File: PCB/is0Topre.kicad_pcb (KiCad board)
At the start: 2 copper layers, 28.6 x 49.7 mm, 32 parts, among them SW1 SW_Push, SW2 EC_SW, U1 ATmega32U4-M, U2 OPA350, Y1 16MHz

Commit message: Updated pic and production to add logo
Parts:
- added G***: LOGO, cipulot_parts:IronMan_small, B.Cu at (110.5, 46.5)

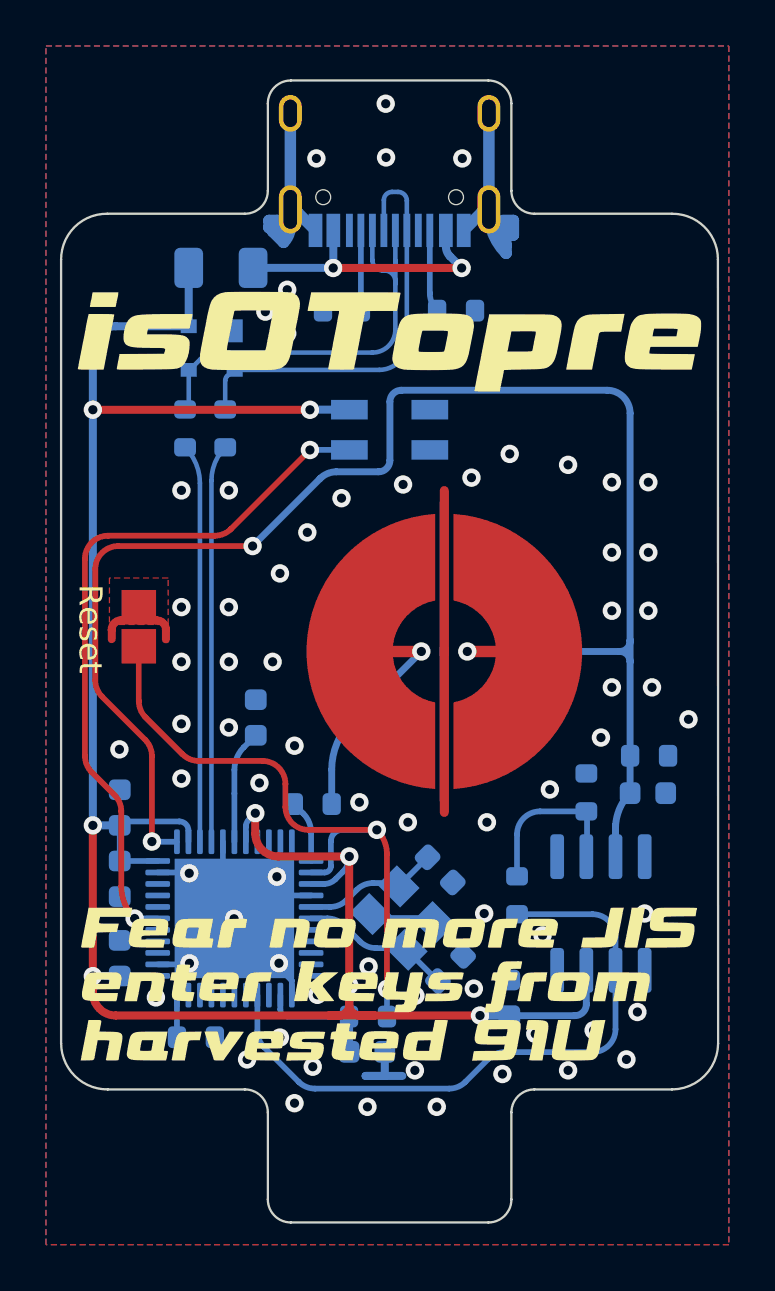
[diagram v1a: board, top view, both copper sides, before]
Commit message: Update to add tape silkscreen
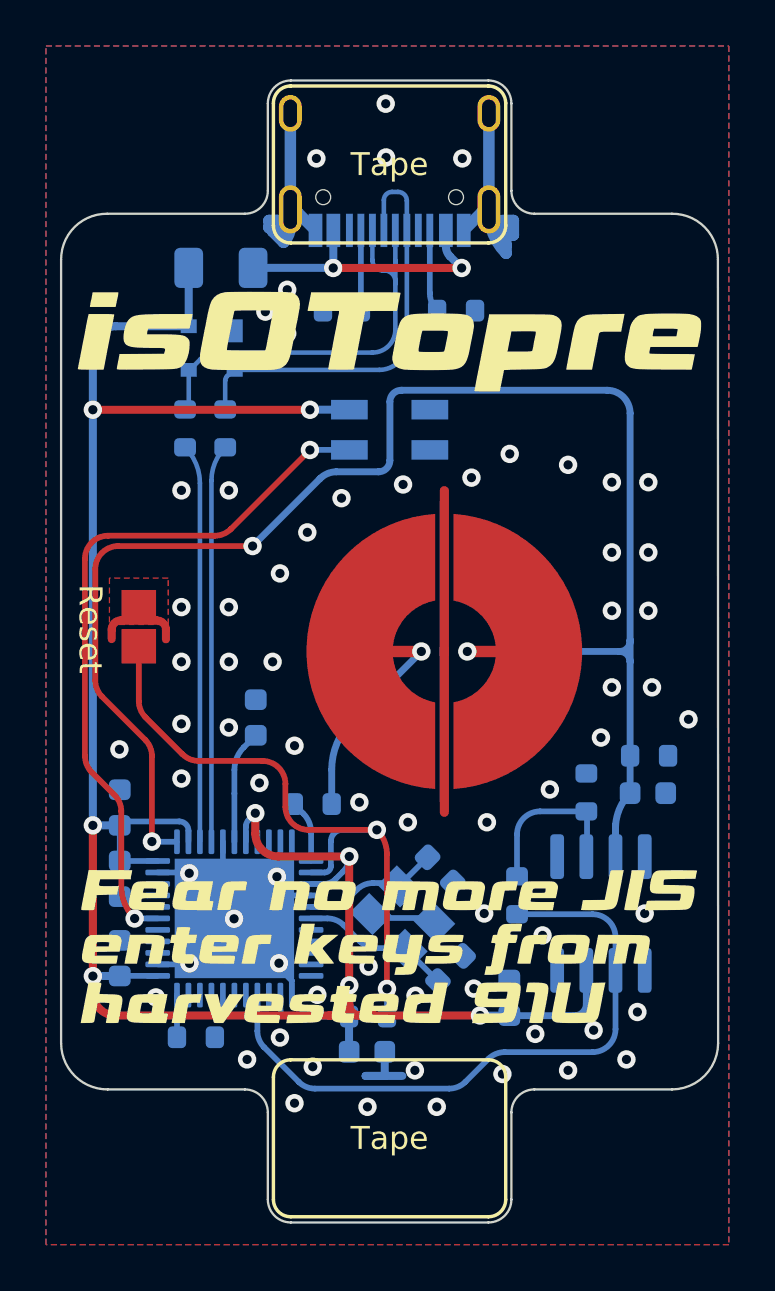
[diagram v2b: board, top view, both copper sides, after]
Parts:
- moved G*** 1.63 mm to (99.5, 71.9)
- moved G*** 1.63 mm to (99.5, 74.4)
- moved G*** 1.63 mm to (99.5, 77.0)
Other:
- board text added: "Tape"
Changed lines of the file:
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@@
   )
   (footprint "LOGO" (layer "F.Cu")
-    (at 99.545928 73.509504)
+    (at 99.545928 71.878991)
     (attr board_only exclude_from_pos_files exclude_from_bom)
     (fp_text reference "G***" (at 0 0) (layer "F.SilkS") hide
@@
   )
   (footprint "LOGO" (layer "F.Cu")
-    (at 99.545928 76.070754)
+    (at 99.545928 74.440241)
     (attr board_only exclude_from_pos_files exclude_from_bom)
     (fp_text reference "G***" (at 0 0) (layer "F.SilkS") hide
@@
   )
   (footprint "LOGO" (layer "F.Cu")
-    (at 99.545928 78.630754)
+    (at 99.545928 77.000241)
     (attr board_only exclude_from_pos_files exclude_from_bom)
     (fp_text reference "G***" (at 0 0) (layer "F.SilkS") hide
@@
     )
   )
+  (gr_arc (start 94.48875 37.64125) (mid 94.708883 37.10903) (end 95.241578 36.890071) (layer "F.SilkS") (width 0.15))
+  (gr_line (start 103.841578 36.890071) (end 95.241578 36.890071) (layer "F.SilkS") (width 0.15))
+  (gr_line (start 104.59875 42.966962) (end 104.59875 37.64125) (layer "F.SilkS") (width 0.15))
+  (gr_arc (start 95.245922 86.10125) (mid 94.711324 85.882899) (end 94.48875 85.350071) (layer "F.SilkS") (width 0.15))
+  (gr_arc (start 94.48875 80.024359) (mid 94.707661 79.492691) (end 95.2384 79.271538) (layer "F.SilkS") (width 0.15))
+  (gr_line (start 95.2384 79.271538) (end 103.845929 79.271538) (layer "F.SilkS") (width 0.15))
+  (gr_arc (start 104.59875 42.966962) (mid 104.379839 43.49863) (end 103.8491 43.719783) (layer "F.SilkS") (width 0.15))
+  (gr_line (start 104.59875 80.021188) (end 104.59875 85.350071) (layer "F.SilkS") (width 0.15))
+  (gr_line (start 94.48875 42.970133) (end 94.48875 37.64125) (layer "F.SilkS") (width 0.15))
+  (gr_arc (start 95.241571 43.719783) (mid 94.709893 43.500876) (end 94.48875 42.970133) (layer "F.SilkS") (width 0.15))
+  (gr_arc (start 103.841578 36.890071) (mid 104.376144 37.108436) (end 104.59875 37.64125) (layer "F.SilkS") (width 0.15))
+  (gr_line (start 95.245922 86.10125) (end 103.845922 86.10125) (layer "F.SilkS") (width 0.15))
+  (gr_arc (start 104.59875 85.350071) (mid 104.37862 85.882288) (end 103.845922 86.10125) (layer "F.SilkS") (width 0.15))
+  (gr_line (start 94.48875 80.024359) (end 94.48875 85.350071) (layer "F.SilkS") (width 0.15))
+  (gr_line (start 103.8491 43.719783) (end 95.241571 43.719783) (layer "F.SilkS") (width 0.15))
+  (gr_arc (start 103.845929 79.271538) (mid 104.377605 79.490442) (end 104.59875 80.021188) (layer "F.SilkS") (width 0.15))
   (gr_line (start 93.245927 42.449999) (end 87.258428 42.449999) (layer "Edge.Cuts") (width 0.1))
   (gr_line (start 95.245922 86.350071) (end 103.845922 86.350071) (layer "Edge.Cuts") (width 0.1))
@@
     (effects (font (size 1 1) (thickness 0.15)) (justify mirror))
   )
+  (gr_text "Tape\n" (at 99.541578 40.304106) (layer "F.SilkS")
+    (effects (font (size 1 1) (thickness 0.15)))
+  )
   (gr_text "Reset" (at 86.517178 60.521801 270) (layer "F.SilkS")
     (effects (font (size 1 1) (thickness 0.15)))
   )
+  (gr_text "Tape" (at 99.541578 82.68563) (layer "F.SilkS")
+    (effects (font (size 1 1) (thickness 0.15)))
+  )

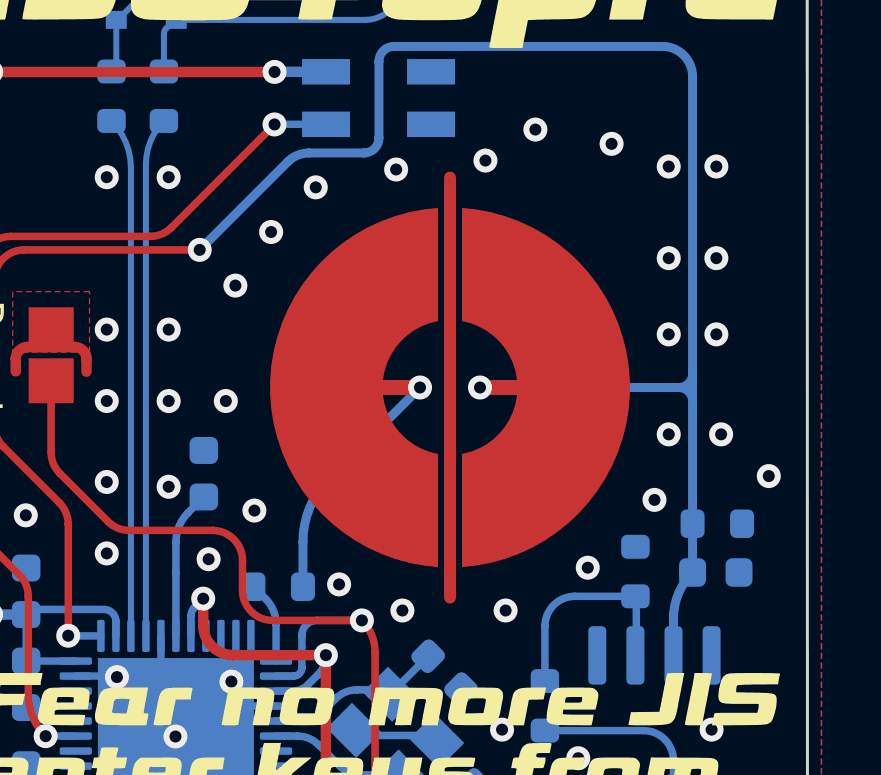
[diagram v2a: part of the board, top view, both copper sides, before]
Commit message: Update for 3d models
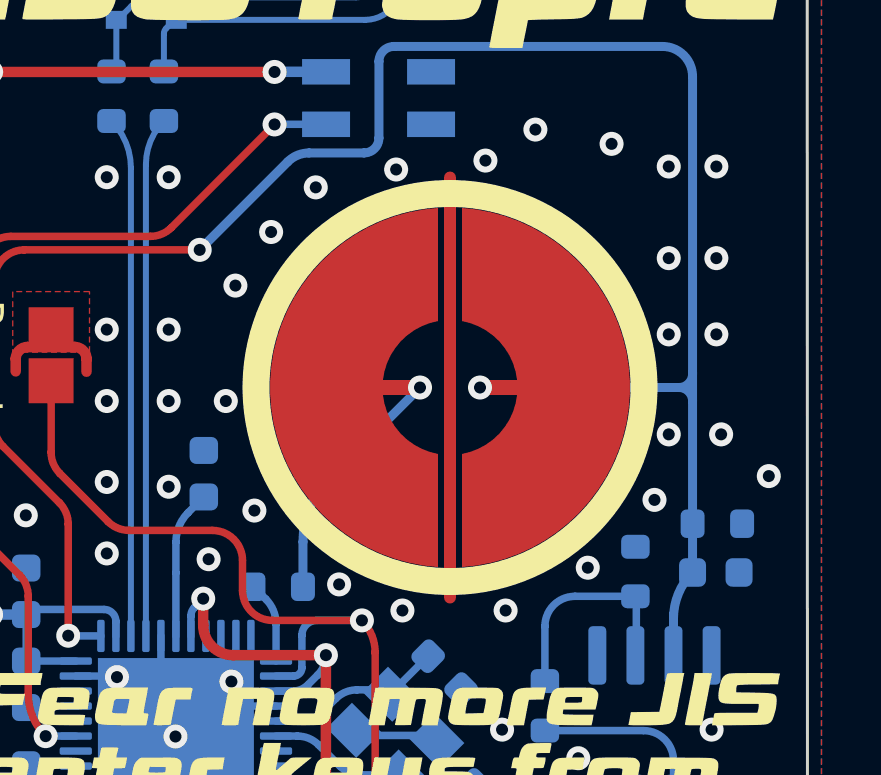
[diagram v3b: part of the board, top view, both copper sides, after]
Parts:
- SW2: footprint cipulot_parts:ecs_pad_no_ring -> cipulot_parts:ecs_pad_2U_no_ring
